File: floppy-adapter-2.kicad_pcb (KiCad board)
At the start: 2 copper layers, 45.7 x 21.7 mm, 2 parts, among them J1 Female Floppy Connector, J2 Edge Connector

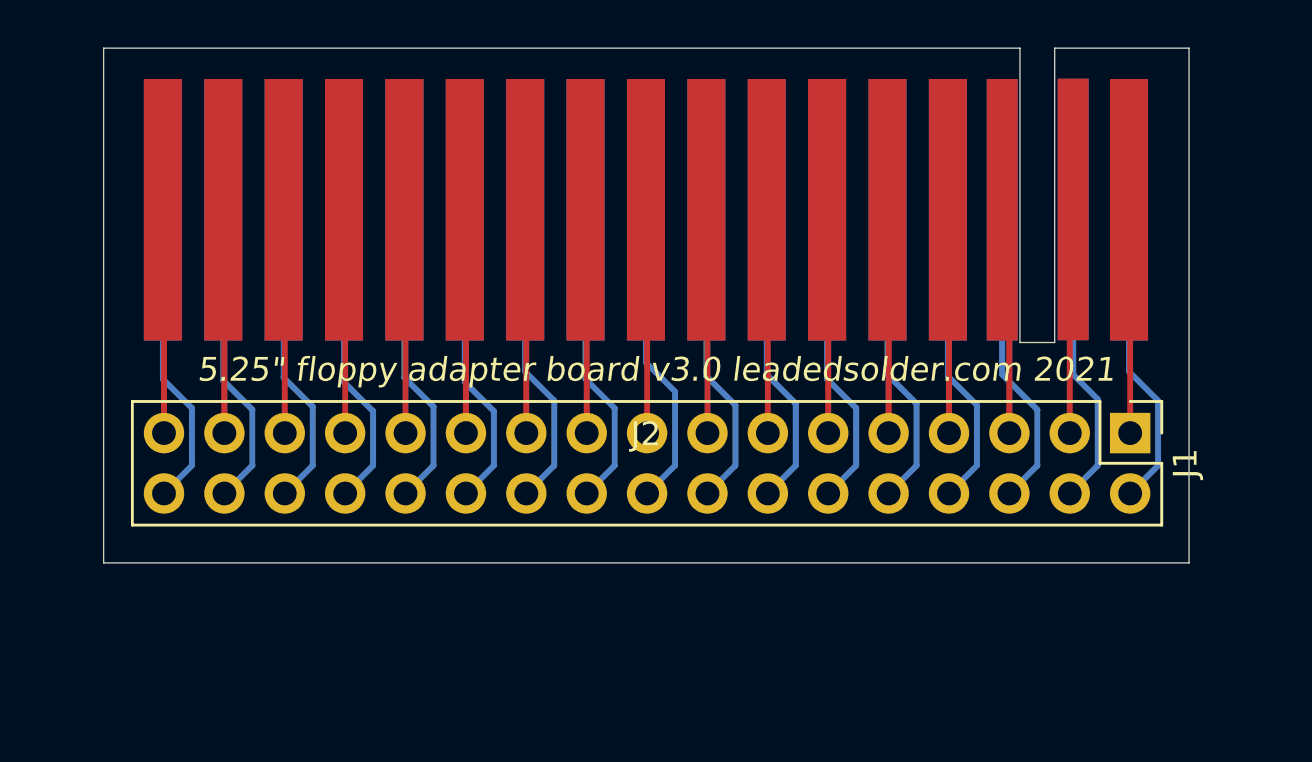
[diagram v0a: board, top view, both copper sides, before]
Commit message: Turn conn around properly
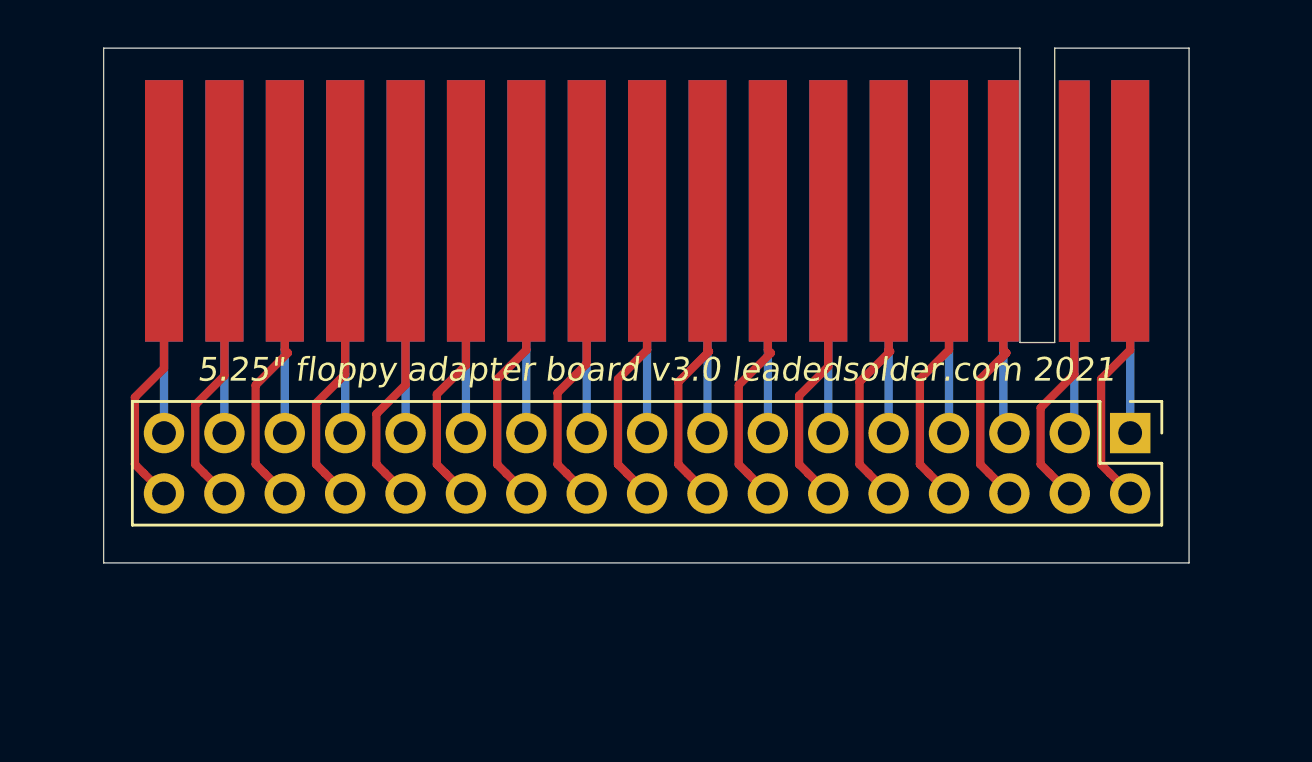
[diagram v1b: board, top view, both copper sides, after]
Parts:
- J2: moved to B.Cu
- moved J2 17.8 mm to (167.5, 71.5)
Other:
- board text added: "mount connector opposite side"

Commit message: Fix my bonehead size mistake
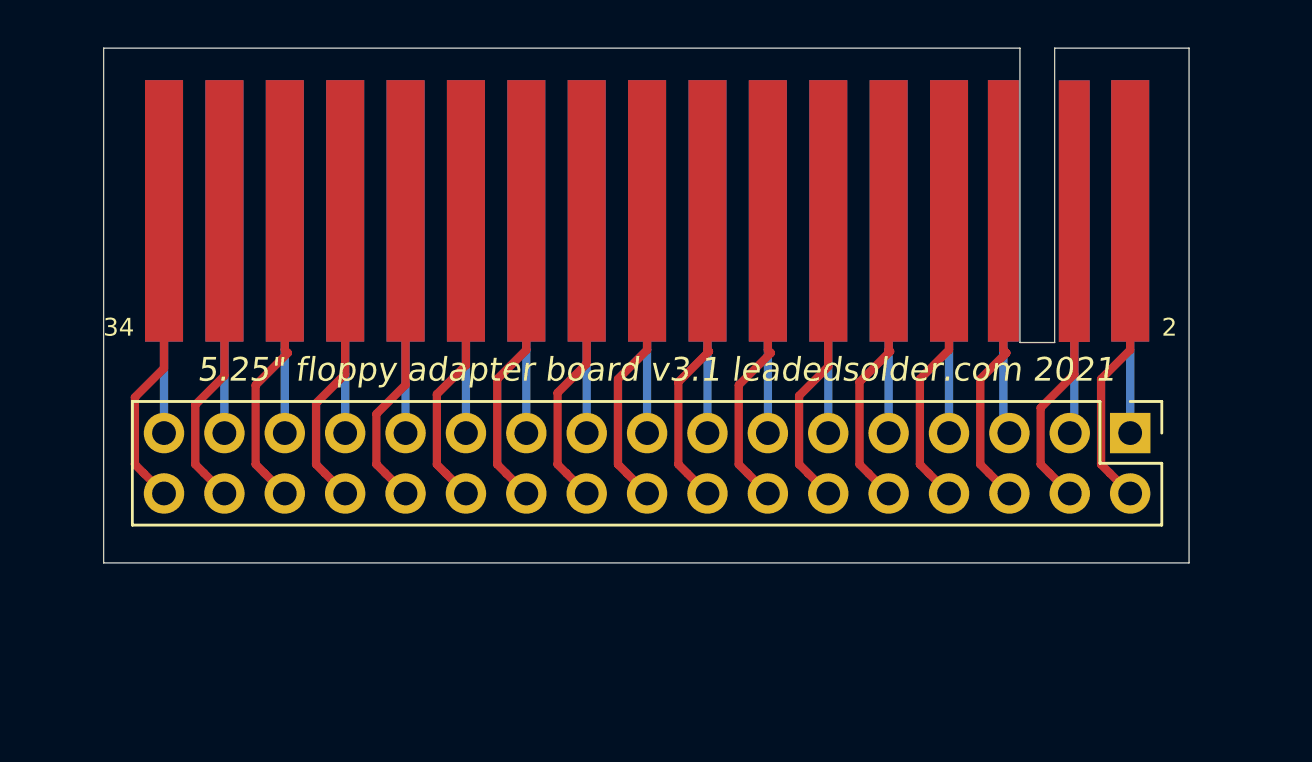
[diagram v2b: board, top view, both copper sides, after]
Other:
- board text added: "2"
- board text added: "34"
- board text added: "5.25" floppy adapter board v3.1 leadedsolder.com 2021"
- board text added: "mount connector this side"
- board text removed: "5.25" floppy adapter board v3.0 leadedsolder.com 2021"
- board text removed: "mount connector opposite side"
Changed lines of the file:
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@@
   (general
     (thickness 1.6)
-    (drawings 18)
+    (drawings 20)
     (tracks 112)
     (zones 0)
@@
   )
   (setup
-    (last_trace_width 0.35)
+    (last_trace_width 0.25)
     (user_trace_width 0.35)
     (trace_clearance 0.2)
@@
     )
   )
-  (gr_text "mount connector opposite side" (at 167.5765 87.122) (layer B.SilkS)
+  (gr_text 34 (at 145.288 85.344) (layer F.SilkS)
+    (effects (font (size 0.75 0.75) (thickness 0.15)))
+  )
+  (gr_text 2 (at 189.484 85.344) (layer F.SilkS)
+    (effects (font (size 0.75 0.75) (thickness 0.15)))
+  )
+  (gr_text "mount connector this side" (at 167.5765 87.122) (layer B.SilkS)
     (effects (font (size 1 1) (thickness 0.15)) (justify mirror))
   )
@@
     (arrow2b (pts (xy 183.1975 54.61) (xy 184.324004 54.023579)))
   )
-  (gr_text "5.25\" floppy adapter board v3.0 leadedsolder.com 2021" (at 167.894 87.122) (layer F.SilkS)
+  (gr_text "5.25\" floppy adapter board v3.1 leadedsolder.com 2021" (at 167.894 87.122) (layer F.SilkS)
     (effects (font (size 1 1) (thickness 0.15) italic))
   )

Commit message: KiCad6; expose DS pins, lengthen board
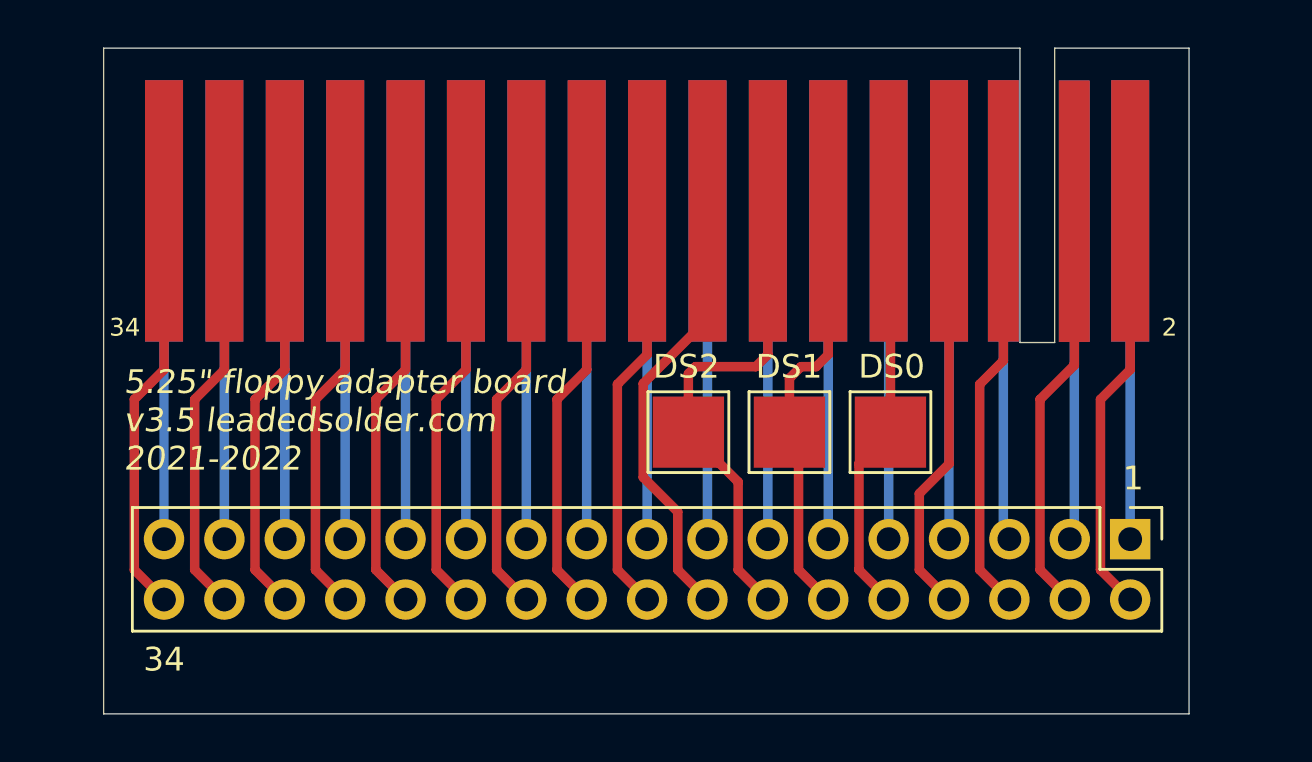
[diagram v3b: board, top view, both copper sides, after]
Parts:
- added TP10: TestPoint, TestPoint:TestPoint_Pad_3.0x3.0mm, F.Cu at (177.8, 89.8)
- added TP12: TestPoint, TestPoint:TestPoint_Pad_3.0x3.0mm, F.Cu at (173.5, 89.8)
- added TP14: TestPoint, TestPoint:TestPoint_Pad_3.0x3.0mm, F.Cu at (169.2, 89.8)
- moved J1 4.46 mm to (187.8, 94.2)
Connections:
- net Net-(J1-Pad10) renamed /DriveSelect0
- net Net-(J1-Pad12) renamed /DriveSelect1
- net Net-(J1-Pad14) renamed /DriveSelect2
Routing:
- net /DriveSelect2: track 13.0 -> 20.6 mm
- net Net-(J1-Pad16): track 13.0 -> 18.6 mm
- net /DriveSelect1: track 12.9 -> 18.1 mm
- net /DriveSelect0: track 13.0 -> 17.4 mm
- net Net-(J1-Pad24): track 12.9 -> 17.4 mm
- net Net-(J1-Pad2): track 12.9 -> 17.4 mm
- net Net-(J1-Pad18): track 12.9 -> 17.4 mm
- net Net-(J1-Pad32): track 12.9 -> 17.4 mm
- net Net-(J1-Pad22): track 12.9 -> 17.4 mm
- net Net-(J1-Pad8): track 12.9 -> 17.4 mm
- net Net-(J1-Pad4): track 13.0 -> 17.4 mm
- net Net-(J1-Pad34): track 12.9 -> 17.4 mm
- net Net-(J1-Pad20): track 12.9 -> 17.4 mm
- net Net-(J1-Pad28): track 12.9 -> 17.4 mm
- net Net-(J1-Pad26): track 12.9 -> 17.4 mm
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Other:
- board size 45.7 x 21.7 mm -> 45.7 x 28 mm
- net class Default removed
- board text added: "1"
- board text added: "33"
- board text added: "5.25{dblquote} floppy adapter board v3.5 leadedsolder.com 2021-2022"
- board text added: "DS0"
- board text added: "DS1"
- board text added: "DS2"
- board text added: "mount connector body this side"
- board text removed: "5.25" floppy adapter board v3.1 leadedsolder.com 2021"
- board text removed: "mount connector this side"

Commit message: KiCad 7
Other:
- rule pad_to_mask_clearance: 0.051 -> 0

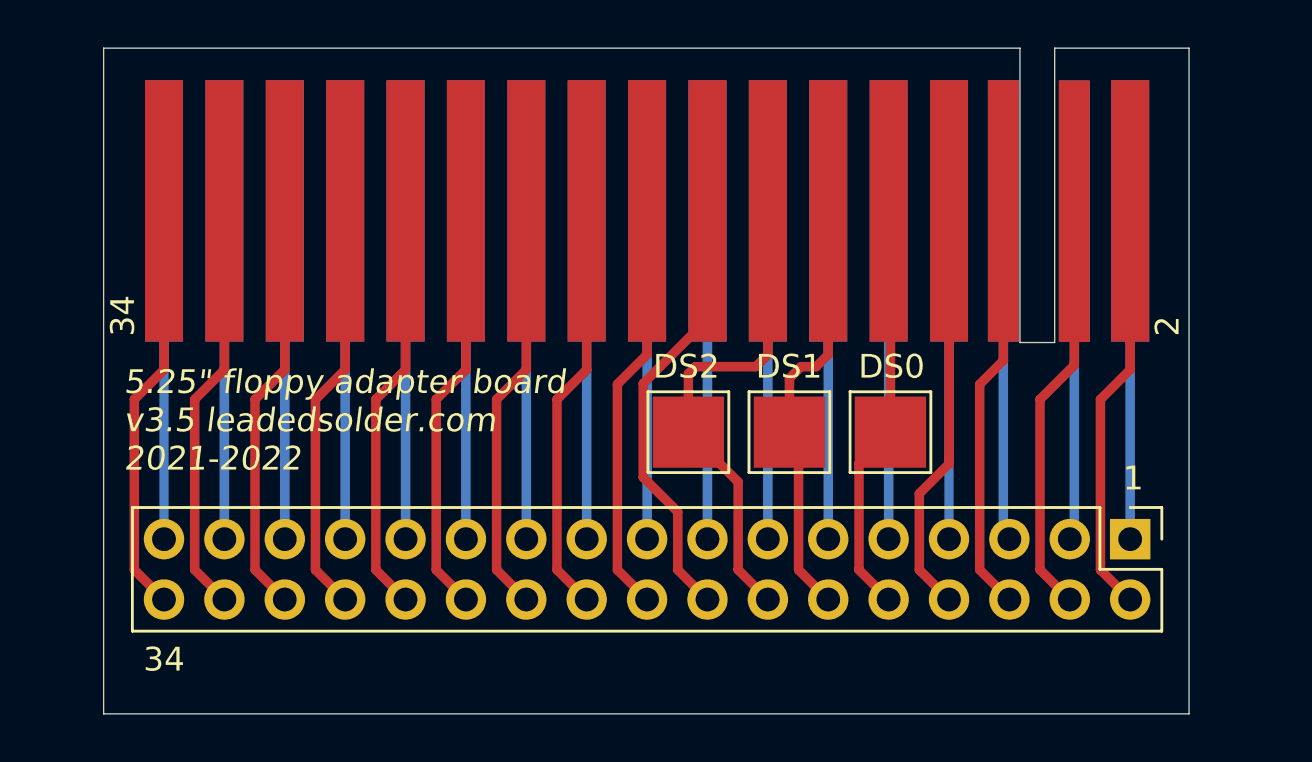
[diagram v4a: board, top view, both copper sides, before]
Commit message: Flip the silkscreen to the other side for the 34-pin connector, finally
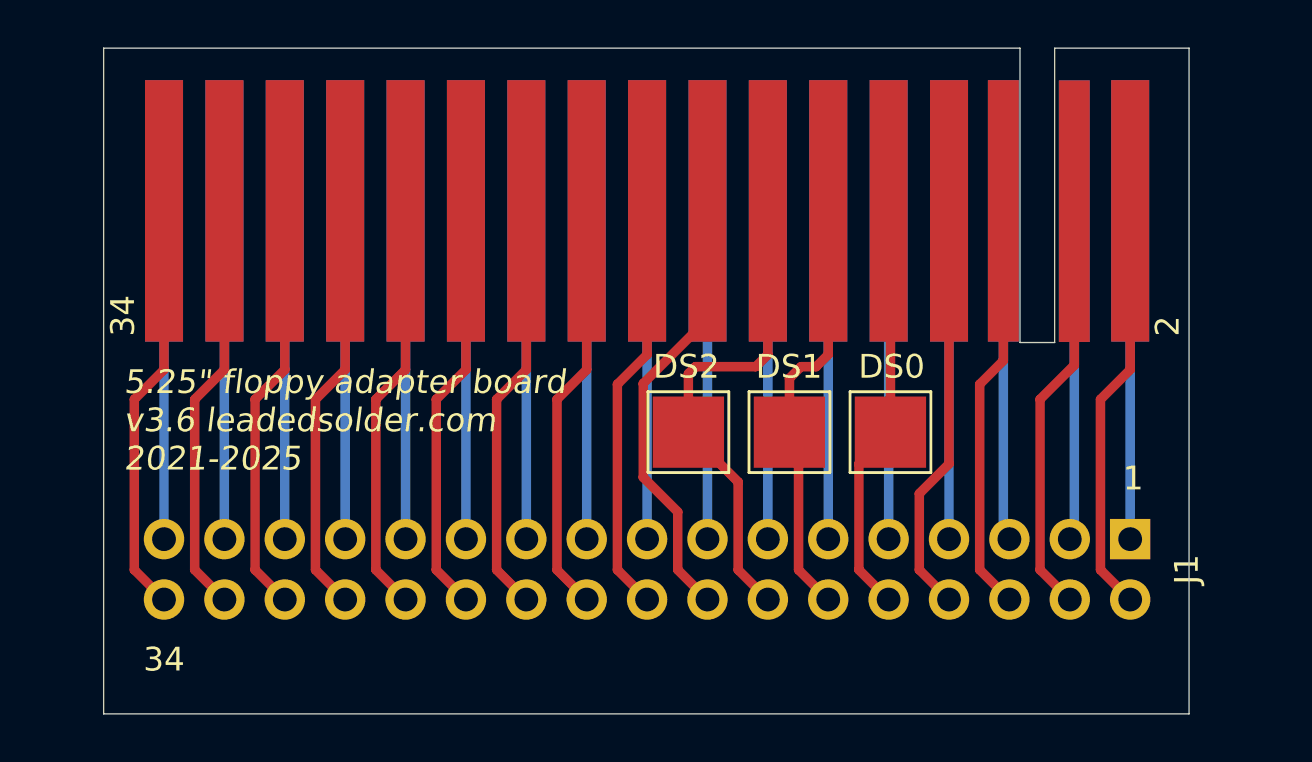
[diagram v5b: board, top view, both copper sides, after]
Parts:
- J1: footprint Connector_PinHeader_2.54mm:PinHeader_2x17_P2.54mm_Vertical -> EdgeConnectors:Floppy_Connector
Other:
- board text added: "5.25{dblquote} floppy adapter board v3.6 leadedsolder.com 2021-2025"
- board text removed: "5.25{dblquote} floppy adapter board v3.5 leadedsolder.com 2021-2022"

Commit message: nice little chamfer
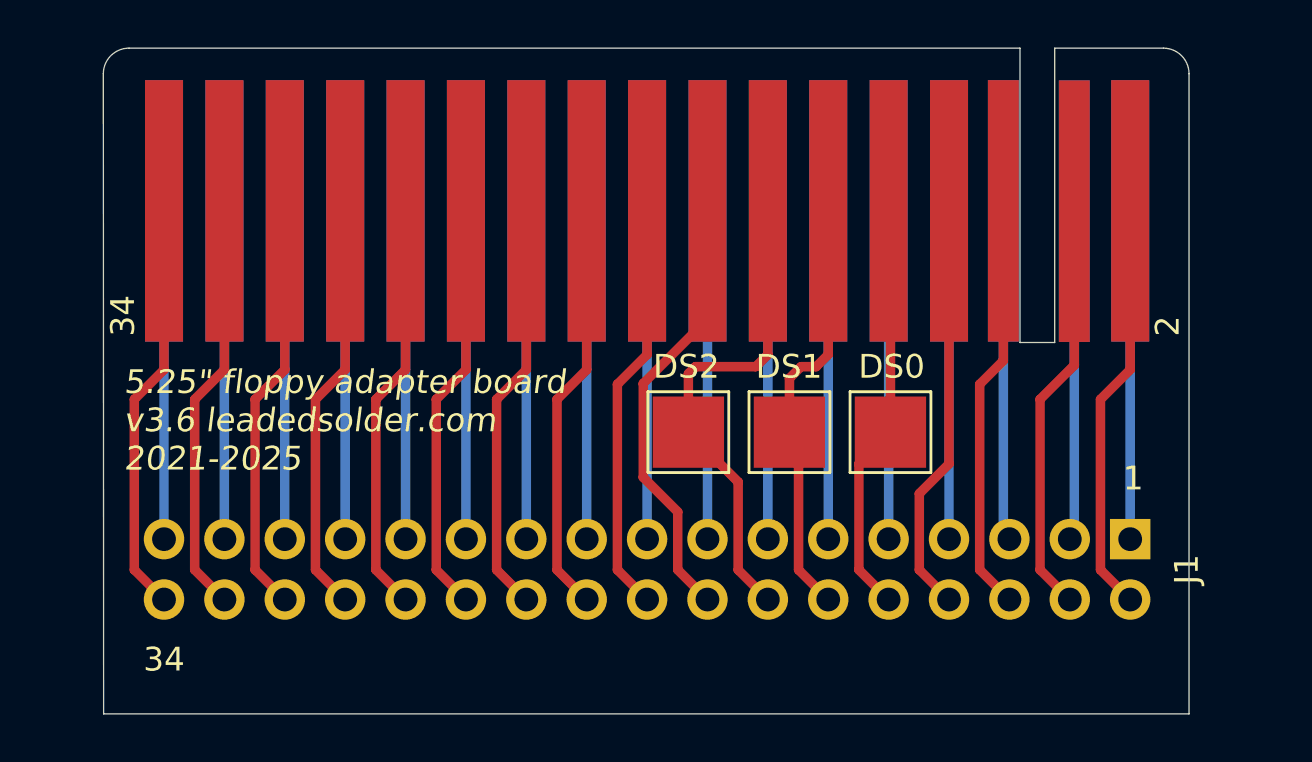
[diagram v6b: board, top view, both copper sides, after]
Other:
- outline, holes or cut-outs redrawn
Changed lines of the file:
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@@
 	)
 	(gr_line
-		(start 144.653 73.5965)
-		(end 144.653 101.6)
+		(start 145.7198 73.5965)
+		(end 183.1975 73.5965)
 		(stroke
 			(width 0.05)
-			(type solid)
+			(type default)
 		)
 		(layer "Edge.Cuts")
 	)
 	(gr_line
-		(start 190.3095 73.5965)
-		(end 190.3095 101.6)
+		(start 189.23 73.5965)
+		(end 184.658 73.5965)
 		(stroke
 			(width 0.05)
-			(type solid)
+			(type default)
 		)
 		(layer "Edge.Cuts")
 	)
 	(gr_line
-		(start 184.658 73.5965)
-		(end 190.3095 73.5965)
+		(start 144.6403 74.676)
+		(end 144.653 101.6)
 		(stroke
 			(width 0.05)
-			(type solid)
+			(type default)
 		)
 		(layer "Edge.Cuts")
@@
 		(layer "Edge.Cuts")
 	)
-	(gr_line
-		(start 183.1975 73.5965)
-		(end 144.653 73.5965)
+	(gr_arc
+		(start 144.6403 74.676)
+		(mid 144.956478 73.912678)
+		(end 145.7198 73.5965)
 		(stroke
 			(width 0.05)
-			(type solid)
+			(type default)
 		)
 		(layer "Edge.Cuts")
+	)
+	(gr_arc
+		(start 189.23 73.5965)
+		(mid 189.993322 73.912678)
+		(end 190.3095 74.676)
+		(stroke
+			(width 0.05)
+			(type default)
+		)
+		(layer "Edge.Cuts")
+	)
+	(gr_line
+		(start 190.3095 74.676)
+		(end 190.3095 101.6)
+		(stroke
+			(width 0.05)
+			(type default)
+		)
+		(layer "Edge.Cuts")

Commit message: Make PCB shorter to avoid bottoming out against the female 34-pin
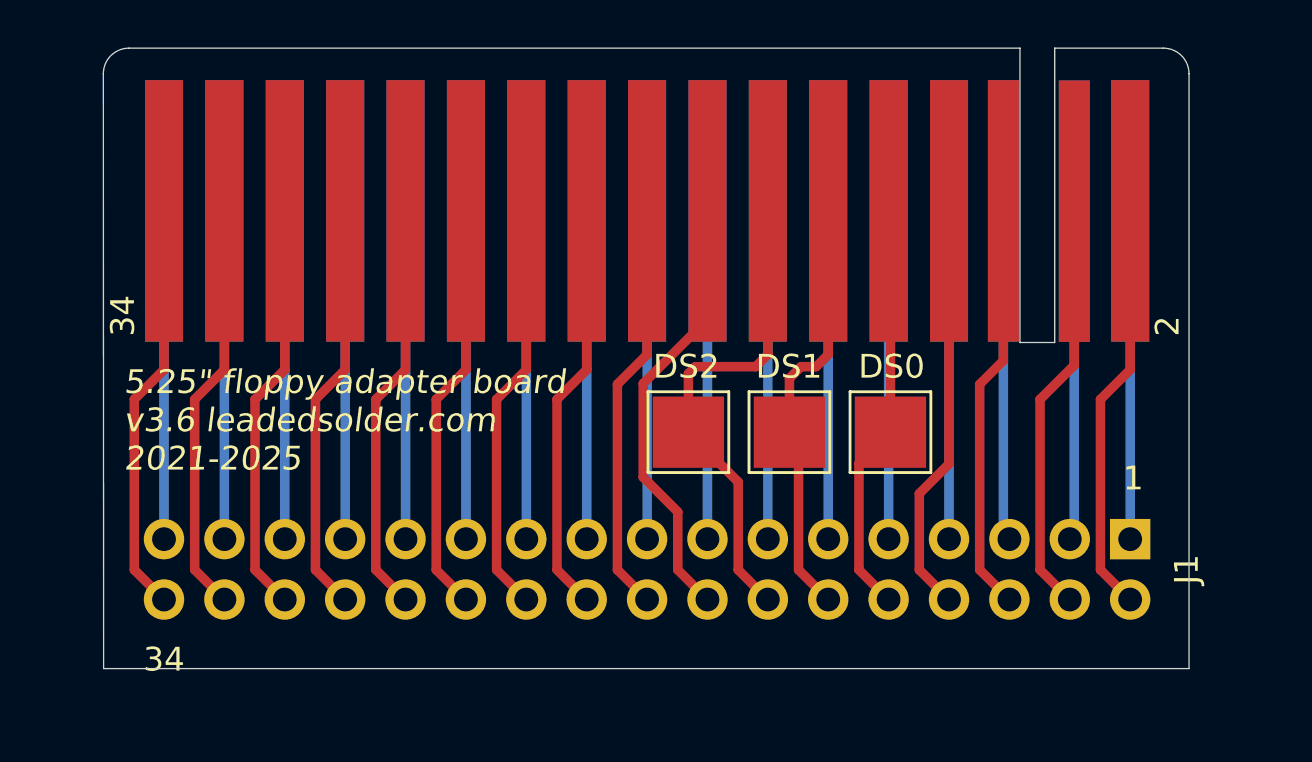
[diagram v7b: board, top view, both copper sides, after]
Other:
- board size 45.7 x 28 mm -> 45.7 x 26.1 mm
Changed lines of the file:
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@@
 	)
 	(gr_line
-		(start 144.653 101.6)
-		(end 190.3095 101.6)
+		(start 144.653 99.695)
+		(end 190.3095 99.695)
 		(stroke
 			(width 0.05)
 			(type solid)
+		)
+		(layer "Edge.Cuts")
+	)
+	(gr_line
+		(start 190.3095 99.695)
+		(end 190.3095 74.676)
+		(stroke
+			(width 0.05)
+			(type default)
+		)
+		(layer "Edge.Cuts")
+	)
+	(gr_line
+		(start 144.6403 74.676)
+		(end 144.653 99.695)
+		(stroke
+			(width 0.05)
+			(type default)
 		)
 		(layer "Edge.Cuts")
@@
 		(start 189.23 73.5965)
 		(end 184.658 73.5965)
-		(stroke
-			(width 0.05)
-			(type default)
-		)
-		(layer "Edge.Cuts")
-	)
-	(gr_line
-		(start 144.6403 74.676)
-		(end 144.653 101.6)
 		(stroke
 			(width 0.05)
@@
 		(stroke
 			(width 0.05)
-			(type default)
-		)
-		(layer "Edge.Cuts")
-	)
-	(gr_line
-		(start 190.3095 74.676)
-		(end 190.3095 101.6)
-		(stroke
-			(width 0.05)
